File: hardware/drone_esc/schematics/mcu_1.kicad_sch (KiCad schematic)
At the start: 0 parts

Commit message: created power schematics, assigned footprints and parts
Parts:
- added U3: STM32G071GBU6, Package_DFN_QFN:QFN-28_4x4mm_P0.5mm, symbol MCU_ST_STM32G0:STM32G071GBUxN
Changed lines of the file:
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@@
 	(generator_version "9.0")
 	(paper "A4")
+	(symbol
+		(lib_id "MCU_ST_STM32G0:STM32G071GBUxN")
+		(at 88.9 115.57 0)
+		(unit 1)
+		(exclude_from_sim no)
+		(in_bom yes)
+		(on_board yes)
+		(dnp no)
+		(property "Reference" "U3"
+			(at 101.6 140.462 0)
+			(effects
+				(font
+					(size 1.27 1.27)
+				)
+				(justify left)
+			)
+		)
+		(property "Value" "STM32G071GBU6"
+			(at 69.088 88.646 0)
+			(effects
+				(font
+					(size 1.27 1.27)
+				)
+				(justify left)
+			)
+		)
+		(property "Footprint" "Package_DFN_QFN:QFN-28_4x4mm_P0.5mm"
+			(at 73.66 138.43 0)
+			(effects
+				(font
+					(size 1.27 1.27)
+				)
+				(justify right)
+				(hide yes)
+			)
+		)
+		(property "Datasheet" "https://www.st.com/resource/en/datasheet/stm32g071gb.pdf"
+			(at 88.9 115.57 0)
+			(effects
+				(font
+					(size 1.27 1.27)
+				)
+				(hide yes)
+			)
+		)
+		(property "Description" "STMicroelectronics Arm Cortex-M0+ MCU, 128KB flash, 36KB RAM, 64 MHz, 1.7-3.6V, 26 GPIO, UFQFPN28"
+			(at 88.9 115.57 0)
+			(effects
+				(font
+					(size 1.27 1.27)
+				)
+				(hide yes)
+			)
+		)
+		(property "JLCPCB part" "C529347"
+			(at 88.9 115.57 0)
+			(effects
+				(font
+					(size 1.27 1.27)
+				)
+				(hide yes)
+			)
+		)
+		(pin "27"
+		)
+		(pin "5"
+		)
+		(pin "23"
+		)
+		(pin "24"
+		)
+		(pin "22"
+		)
+		(pin "25"
+		)
+		(pin "1"
+		)
+		(pin "2"
+		)
+		(pin "14"
+		)
+		(pin "26"
+		)
+		(pin "17"
+		)
+		(pin "3"
+		)
+		(pin "9"
+		)
+		(pin "11"
+		)
+		(pin "12"
+		)
+		(pin "16"
+		)
+		(pin "21"
+		)
+		(pin "28"
+		)
+		(pin "6"
+		)
+		(pin "10"
+		)
+		(pin "19"
+		)
+		(pin "13"
+		)
+		(pin "7"
+		)
+		(pin "15"
+		)
+		(pin "8"
+		)
+		(pin "18"
+		)
+		(pin "20"
+		)
+		(pin "4"
+		)
+		(instances
+			(project ""
+				(path "/b5a13fd4-6868-4fff-a56c-eae40f1d53c7/91ef4a31-1dcb-46c6-9edf-7447de09e4c1"
+					(reference "U3")
+					(unit 1)
+				)
+			)
+		)
+	)
 )

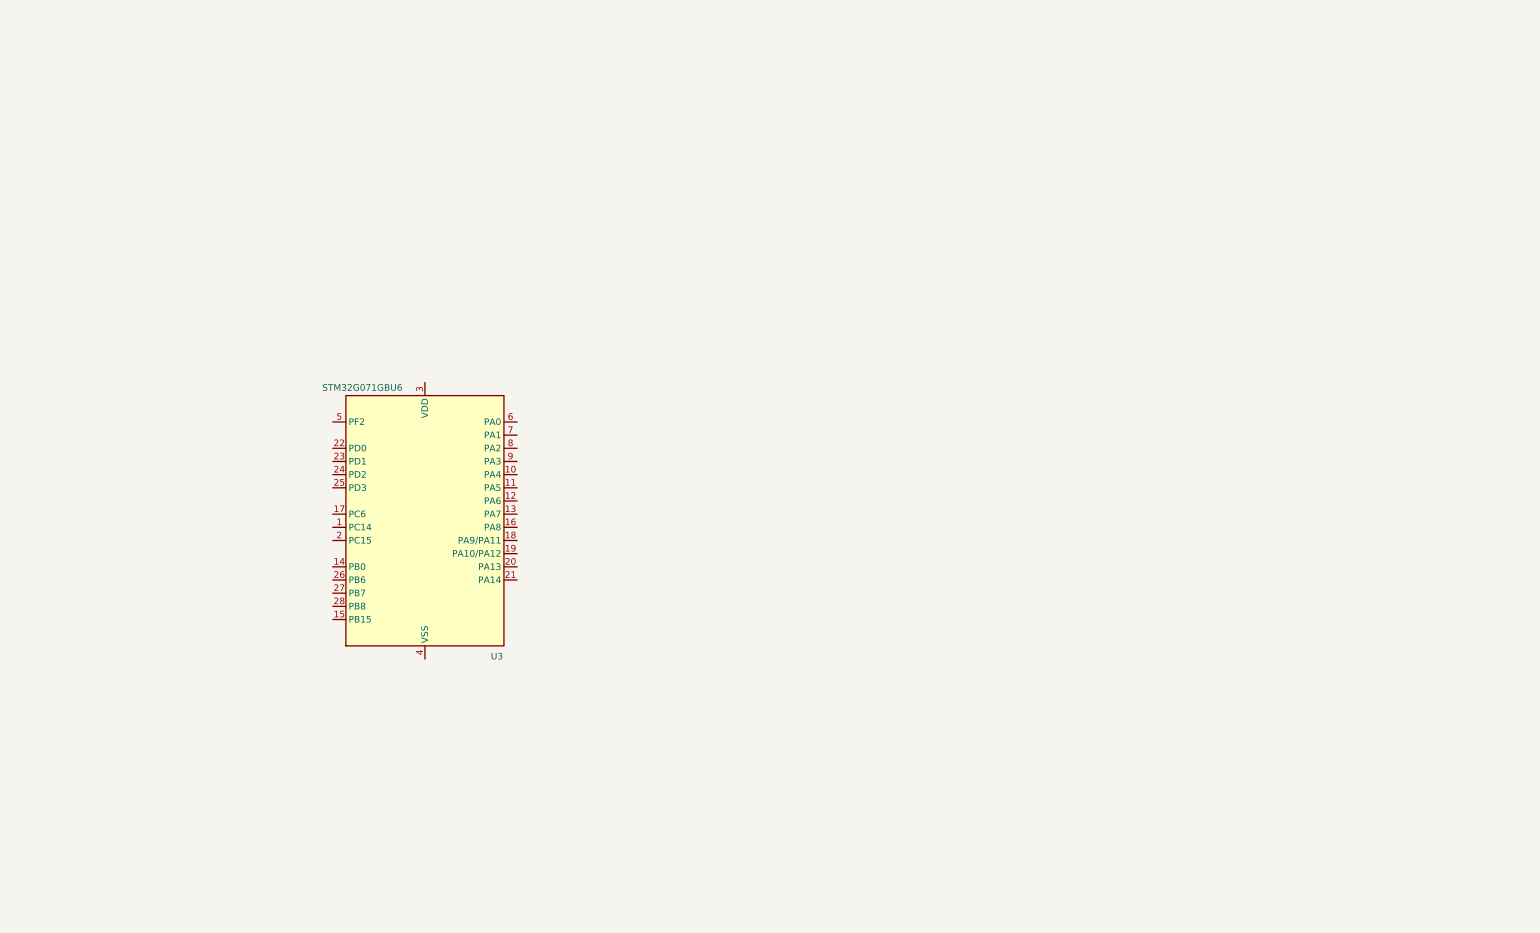
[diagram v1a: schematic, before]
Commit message: finished power section and one esc. need to finish the component assinment for jlcpcb and the rest of the esc
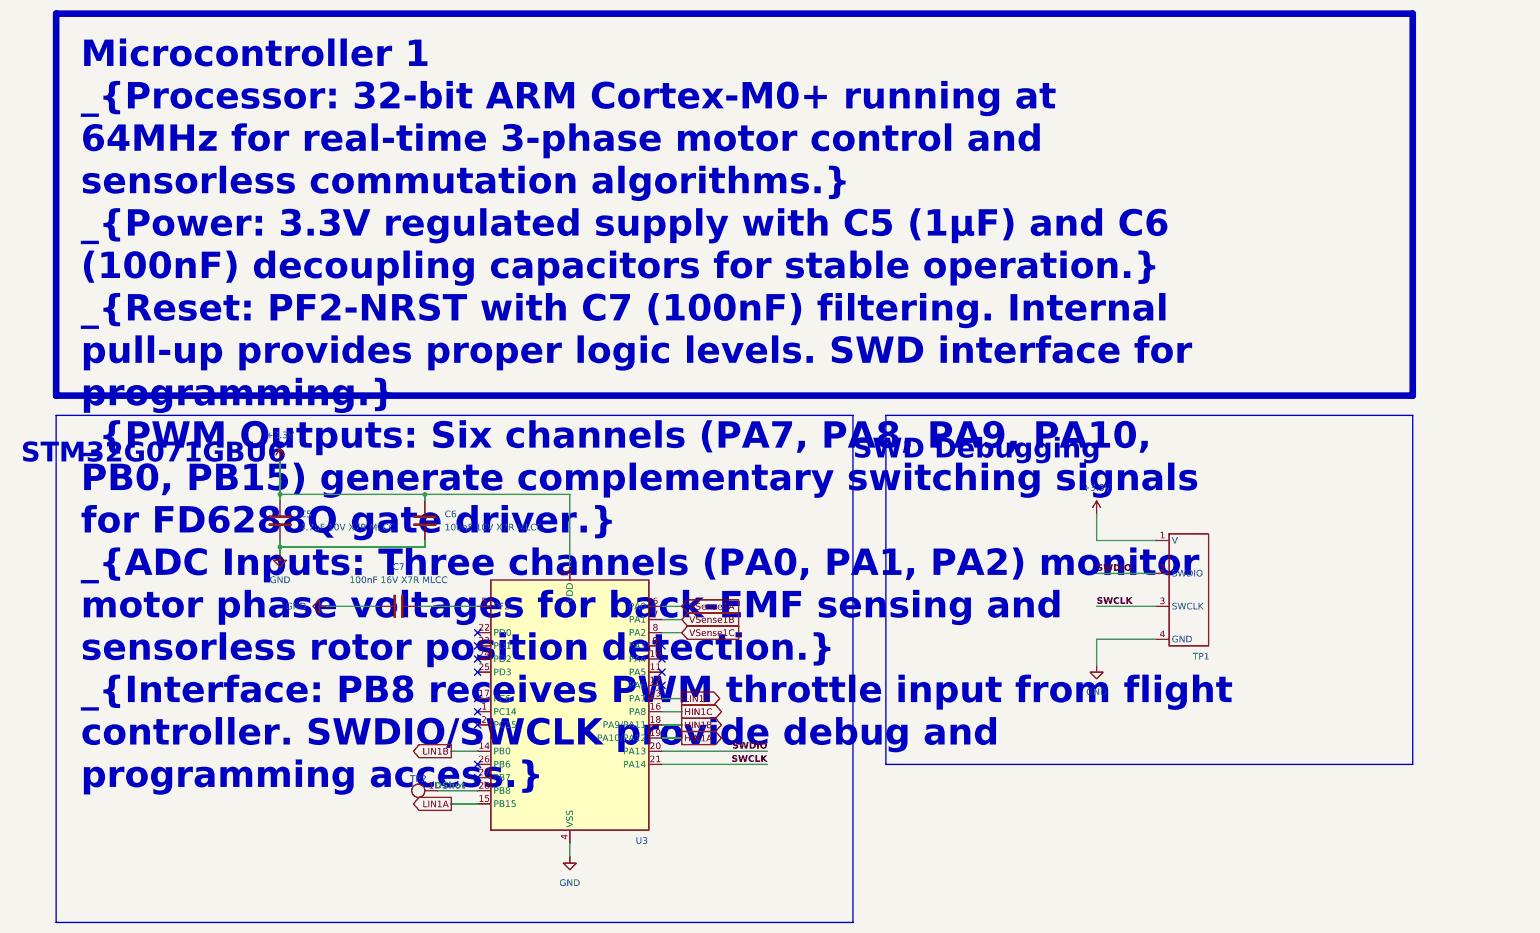
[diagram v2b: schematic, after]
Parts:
- added C5: 4.7uF 10V X7R MLCC, Capacitor_SMD:C_0603_1608Metric, symbol Device:C
- added C6: 100nF 10V X7R MLCC, Capacitor_SMD:C_0402_1005Metric, symbol Device:C
- added C7: 100nF 16V X7R MLCC, Capacitor_SMD:C_01005_0402Metric, symbol Device:C
- added TP1: ~, Drone_components:1.27 test pad, symbol Drone_components:1.27_test_pad
- added TP2: DShot, Drone_components:Rectangle test point, symbol Drone_components:Rectangle_test_point
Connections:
- net LIN1C: now reaches U3.13 (PA7)
- net LIN1B: now reaches U3.14 (PB0)
- net LIN1A: now reaches U3.15 (PB15)
- net HIN1C: now reaches U3.16 (PA8)
- net HIN1B: now reaches U3.18 (PA9/PA11)
- net HIN1A: now reaches U3.19 (PA10/PA12)
- net SWDIO: now reaches U3.20 (PA13)
- net SWDIO: now also TP1.2 (SWDIO)
- net SWCLK: now reaches U3.21 (PA14)
- net SWCLK: now also TP1.3 (SWCLK)
- net at U3.28 (PB8): now also TP2.1
- net +3.3V: now reaches U3.3 (VDD)
- net +3.3V: now also C5.1, C6.1, TP1.1 (V)
- net GND: now reaches U3.4 (VSS)
- net GND: now also C5.2, C6.2, C7.1, TP1.4 (GND)
- net at U3.5 (PF2): now also C7.2
- net VSense1A: now reaches U3.6 (PA0)
- net VSense1B: now reaches U3.7 (PA1)
- net VSense1C: now reaches U3.8 (PA2)
- no-connect marks 0 -> 13
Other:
- note added: "STM32G071GBU6"
- note added: "SWD Debugging"
- moved on the sheet: U3

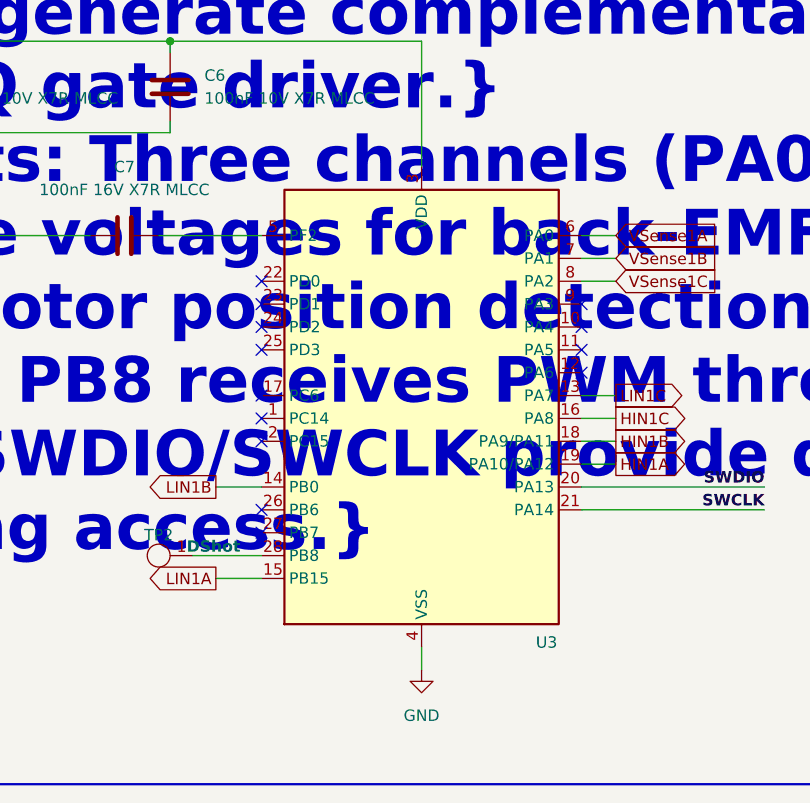
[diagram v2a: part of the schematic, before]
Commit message: finished the schematics and started to work on the PCB. need to find mcu model and finish the sheet description
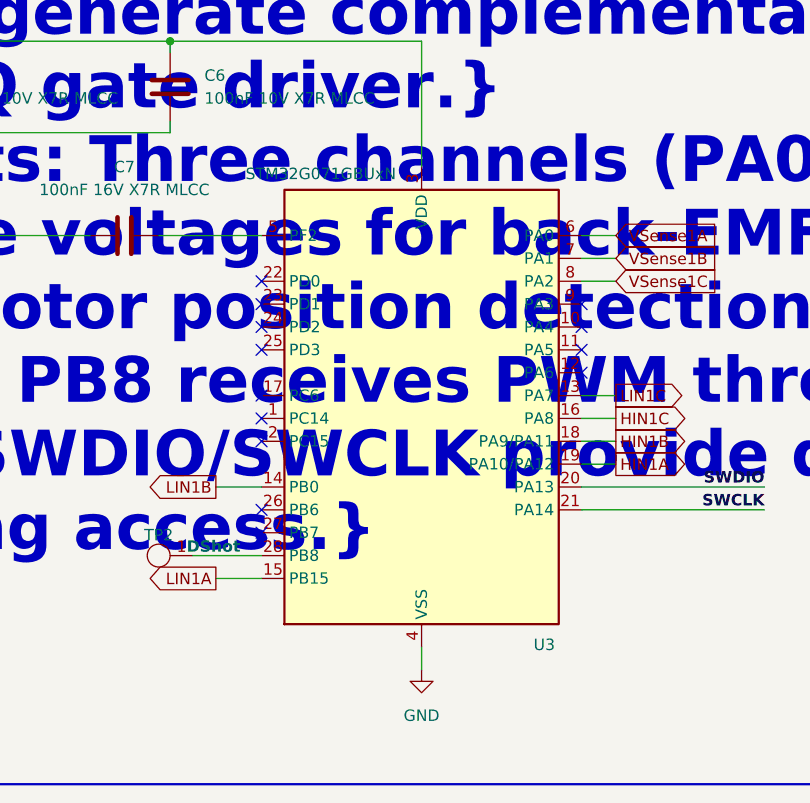
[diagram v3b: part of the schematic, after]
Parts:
- U3: value STM32G071GBU6 -> STM32G071GBUxN; JLCPCB part C529347 -> (none)
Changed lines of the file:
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@@
+	)
+	(symbol
+		(lib_id "MCU_ST_STM32G0:STM32G071GBUxN")
+		(at 116.84 151.13 0)
+		(unit 1)
+		(exclude_from_sim no)
+		(in_bom yes)
+		(on_board yes)
+		(dnp no)
+		(property "Reference" "U3"
+			(at 129.286 176.276 0)
+			(effects
+				(font
+					(size 1.27 1.27)
+				)
+				(justify left)
+			)
+		)
+		(property "Value" "STM32G071GBUxN"
+			(at 97.282 123.952 0)
+			(effects
+				(font
+					(size 1.27 1.27)
+				)
+				(justify left)
+			)
+		)
+		(property "Footprint" "Package_DFN_QFN:QFN-28_4x4mm_P0.5mm"
+			(at 101.6 173.99 0)
+			(effects
+				(font
+					(size 1.27 1.27)
+				)
+				(justify right)
+				(hide yes)
+			)
+		)
+		(property "Datasheet" "https://www.st.com/resource/en/datasheet/stm32g071gb.pdf"
+			(at 116.84 151.13 0)
+			(effects
+				(font
+					(size 1.27 1.27)
+				)
+				(hide yes)
+			)
+		)
+		(property "Description" "STMicroelectronics Arm Cortex-M0+ MCU, 128KB flash, 36KB RAM, 64 MHz, 1.7-3.6V, 26 GPIO, UFQFPN28"
+			(at 116.84 151.13 0)
+			(effects
+				(font
+					(size 1.27 1.27)
+				)
+				(hide yes)
+			)
+		)
+		(pin "27"
+		)
+		(pin "13"
+		)
+		(pin "17"
+		)
+		(pin "5"
+		)
+		(pin "24"
+		)
+		(pin "26"
+		)
+		(pin "22"
+		)
+		(pin "6"
+		)
+		(pin "1"
+		)
+		(pin "12"
+		)
+		(pin "2"
+		)
+		(pin "25"
+		)
+		(pin "15"
+		)
+		(pin "9"
+		)
+		(pin "10"
+		)
+		(pin "14"
+		)
+		(pin "28"
+		)
+		(pin "3"
+		)
+		(pin "4"
+		)
+		(pin "23"
+		)
+		(pin "7"
+		)
+		(pin "8"
+		)
+		(pin "11"
+		)
+		(pin "21"
+		)
+		(pin "20"
+		)
+		(pin "16"
+		)
+		(pin "18"
+		)
+		(pin "19"
+		)
+		(instances
+			(project ""
+				(path "/b5a13fd4-6868-4fff-a56c-eae40f1d53c7/91ef4a31-1dcb-46c6-9edf-7447de09e4c1"
+					(reference "U3")
+					(unit 1)
+				)
+			)
+		)
 	)
 	(symbol
@@
 					(unit 1)
 				)
-			)
-		)
-	)
-	(symbol
-		(lib_id "MCU_ST_STM32G0:STM32G071GBUxN")
-		(at 116.84 151.13 0)
-		(unit 1)
-		(exclude_from_sim no)
-		(in_bom yes)
-		(on_board yes)
-		(dnp no)
-		(property "Reference" "U3"
-			(at 129.54 176.022 0)
-			(effects
-				(font
-					(size 1.27 1.27)
-				)
-				(justify left)
-			)
-		)
-		(property "Value" "STM32G071GBU6"
-			(at 97.028 124.206 0)
-			(effects
-				(font
-					(size 1.27 1.27)
-				)
-				(justify left)
-				(hide yes)
-			)
-		)
-		(property "Footprint" "Package_DFN_QFN:QFN-28_4x4mm_P0.5mm"
-			(at 101.6 173.99 0)
-			(effects
-				(font
-					(size 1.27 1.27)
-				)
-				(justify right)
-				(hide yes)
-			)
-		)
-		(property "Datasheet" "https://www.st.com/resource/en/datasheet/stm32g071gb.pdf"
-			(at 116.84 151.13 0)
-			(effects
-				(font
-					(size 1.27 1.27)
-				)
-				(hide yes)
-			)
-		)
-		(property "Description" "STMicroelectronics Arm Cortex-M0+ MCU, 128KB flash, 36KB RAM, 64 MHz, 1.7-3.6V, 26 GPIO, UFQFPN28"
-			(at 116.84 151.13 0)
-			(effects
-				(font
-					(size 1.27 1.27)
-				)
-				(hide yes)
-			)
-		)
-		(property "JLCPCB part" "C529347"
-			(at 116.84 151.13 0)
-			(effects
-				(font
-					(size 1.27 1.27)
-				)
-				(hide yes)
-			)
-		)
-		(pin "27"
-		)
-		(pin "5"
-		)
-		(pin "23"
-		)
-		(pin "24"
-		)
-		(pin "22"
-		)
-		(pin "25"
-		)
-		(pin "1"
-		)
-		(pin "2"
-		)
-		(pin "14"
-		)
-		(pin "26"
-		)
-		(pin "17"
-		)
-		(pin "3"
-		)
-		(pin "9"
-		)
-		(pin "11"
-		)
-		(pin "12"
-		)
-		(pin "16"
-		)
-		(pin "21"
-		)
-		(pin "28"
-		)
-		(pin "6"
-		)
-		(pin "10"
-		)
-		(pin "19"
-		)
-		(pin "13"
-		)
-		(pin "7"
-		)
-		(pin "15"
-		)
-		(pin "8"
-		)
-		(pin "18"
-		)
-		(pin "20"
-		)
-		(pin "4"
-		)
-		(instances
-			(project ""
-				(path "/b5a13fd4-6868-4fff-a56c-eae40f1d53c7/91ef4a31-1dcb-46c6-9edf-7447de09e4c1"
-					(reference "U3")
-					(unit 1)
-				)

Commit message: finnished component placement
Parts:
- C5: value 4.7uF 10V X7R MLCC -> 4.7uF 10V X5R MLCC; footprint Capacitor_SMD:C_0603_1608Metric -> Capacitor_SMD:C_0402_1005Metric; JLCPCB part C108342 -> C23733
- C7: footprint Capacitor_SMD:C_01005_0402Metric -> Capacitor_SMD:C_0402_1005Metric
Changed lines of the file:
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@@
 			)
 		)
-		(property "Footprint" "Capacitor_SMD:C_01005_0402Metric"
+		(property "Footprint" "Capacitor_SMD:C_0402_1005Metric"
 			(at 87.63 129.8448 0)
 			(effects
@@
 			)
 		)
-		(property "Value" "4.7uF 10V X7R MLCC"
+		(property "Value" "4.7uF 10V X5R MLCC"
 			(at 64.77 115.5699 0)
 			(effects
@@
 			)
 		)
-		(property "Footprint" "Capacitor_SMD:C_0603_1608Metric"
+		(property "Footprint" "Capacitor_SMD:C_0402_1005Metric"
 			(at 61.9252 118.11 0)
 			(effects
@@
 			)
 		)
-		(property "JLCPCB part" "C108342"
+		(property "JLCPCB part" "C23733"
 			(at 60.96 114.3 0)
 			(effects
